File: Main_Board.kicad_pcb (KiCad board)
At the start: 2 copper layers, 95 x 95 mm, 61 parts, among them J1 DAC_12-bits, J2 Measurement_Header, Q1 Q_PNP_BCE, Q2 Q_NPN_BCE, U1 AD667, U2 LF356

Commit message: All traced
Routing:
- net /+15V: track 135.9 -> 210.0 mm, vias 1 -> 3
- net /-15V: track 118.5 -> 175.2 mm
- net GND: track 423.9 -> 480.5 mm
- net /Vout: track 13.5 -> 38.4 mm
- net /-5V: track 62.5 -> 69.4 mm, vias 0 -> 1
- net /-3V: track 77.0 -> 83.5 mm
- net Net-(RV1-Pad1): track 25.2 -> 29.2 mm
- net /Vin: track 199.4 -> 201.6 mm
- net Net-(RV1-Pad2): track 29.6 -> 31.2 mm
- net /MSP430_P1.6_Bit6: track 9.63 -> 9.00 mm

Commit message: Final
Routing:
- net GND: track 480.5 -> 492.6 mm
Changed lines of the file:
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@@
     (thickness 1.6)
     (drawings 17)
-    (tracks 481)
+    (tracks 482)
     (zones 0)
     (modules 61)
@@
   (segment (start 31.9 124.9) (end 37 130) (width 0.25) (layer F.Cu) (net 1))
   (segment (start 31.9 121.0375) (end 31.9 124.9) (width 0.25) (layer F.Cu) (net 1))
-  (segment (start 21.125 139.7) (end 18.7 142.125) (width 0.25) (layer F.Cu) (net 1))
   (segment (start 23.91 139.7) (end 21.125 139.7) (width 0.25) (layer F.Cu) (net 1))
   (segment (start 37 130.175997) (end 37 130) (width 0.25) (layer F.Cu) (net 1))
@@
   (segment (start 18.7 142.125) (end 22.5125 145.9375) (width 0.25) (layer F.Cu) (net 1))
   (segment (start 18.214473 142.610527) (end 18.7 142.125) (width 0.25) (layer F.Cu) (net 1))
-  (segment (start 17.67499 143.15001) (end 18.214473 142.610527) (width 0.25) (layer F.Cu) (net 1))
-  (segment (start 17.67499 144.47934) (end 17.67499 143.15001) (width 0.25) (layer F.Cu) (net 1))
-  (segment (start 21.09205 147.8964) (end 17.67499 144.47934) (width 0.25) (layer F.Cu) (net 1))
-  (segment (start 30.8508 147.8964) (end 21.09205 147.8964) (width 0.25) (layer F.Cu) (net 1))
   (segment (start 64.6826 117.5506) (end 64.7304 117.5028) (width 0.25) (layer F.Cu) (net 1))
   (segment (start 60.26 117.5506) (end 64.6826 117.5506) (width 0.25) (layer F.Cu) (net 1))
@@
   (segment (start 90.8658 112.1658) (end 80.5304 112.1658) (width 0.25) (layer F.Cu) (net 1))
   (segment (start 93.3 114.6) (end 90.8658 112.1658) (width 0.25) (layer F.Cu) (net 1))
-  (segment (start 34.894563 150.327637) (end 35.4508 149.7714) (width 0.25) (layer F.Cu) (net 2))
-  (segment (start 30.8508 149.7714) (end 31.407037 150.327637) (width 0.25) (layer F.Cu) (net 2))
+  (segment (start 17.2 139.7) (end 21.125 139.7) (width 0.25) (layer F.Cu) (net 1))
+  (segment (start 16.1 140.8) (end 17.2 139.7) (width 0.25) (layer F.Cu) (net 1))
+  (segment (start 16.1 145.5) (end 16.1 140.8) (width 0.25) (layer F.Cu) (net 1))
+  (segment (start 30.8508 147.8964) (end 18.4964 147.8964) (width 0.25) (layer F.Cu) (net 1))
+  (segment (start 18.4964 147.8964) (end 16.1 145.5) (width 0.25) (layer F.Cu) (net 1))
+  (segment (start 23.71 139.7) (end 23.91 139.7) (width 0.25) (layer F.Cu) (net 1))
+  (segment (start 21.285 142.125) (end 23.71 139.7) (width 0.25) (layer F.Cu) (net 1))
+  (segment (start 18.7 142.125) (end 21.285 142.125) (width 0.25) (layer F.Cu) (net 1))
   (via (at 43.0508 156.7714) (size 0.8) (drill 0.4) (layers F.Cu B.Cu) (net 2))
   (segment (start 45.5758 156.7714) (end 43.0508 156.7714) (width 0.25) (layer F.Cu) (net 2))
@@
   (segment (start 21.3336 146.6336) (end 32.1168 146.6336) (width 0.25) (layer F.Cu) (net 2))
   (segment (start 32.1168 146.6336) (end 32.5232 147.04) (width 0.25) (layer F.Cu) (net 2))
-  (segment (start 32.5232 147.04) (end 32.5232 150.3166) (width 0.25) (layer F.Cu) (net 2))
-  (segment (start 31.407037 150.327637) (end 32.5232 150.3166) (width 0.25) (layer F.Cu) (net 2))
-  (segment (start 32.5232 150.3166) (end 34.894563 150.327637) (width 0.25) (layer F.Cu) (net 2))
+  (segment (start 31.6508 149.7714) (end 35.4508 149.7714) (width 0.25) (layer F.Cu) (net 2))
+  (segment (start 30.8508 149.7714) (end 31.6508 149.7714) (width 0.25) (layer F.Cu) (net 2))
+  (segment (start 32.5232 148.099) (end 30.8508 149.7714) (width 0.25) (layer F.Cu) (net 2))
+  (segment (start 32.5232 147.04) (end 32.5232 148.099) (width 0.25) (layer F.Cu) (net 2))
   (segment (start 29.241333 141.416333) (end 29.19233 141.416333) (width 0.25) (layer F.Cu) (net 3))
   (segment (start 47.4508 150.9014) (end 47.4508 156.7714) (width 0.25) (layer F.Cu) (net 3))
@@
   (segment (start 54.2133 168.8714) (end 54.1508 168.8089) (width 0.25) (layer F.Cu) (net 3))
   (segment (start 61.2408 168.8714) (end 54.2133 168.8714) (width 0.25) (layer F.Cu) (net 3))
-  (segment (start 54.1508 169.6714) (end 54.1508 168.8089) (width 0.25) (layer F.Cu) (net 3))
-  (segment (start 58.7508 174.2714) (end 54.1508 169.6714) (width 0.25) (layer F.Cu) (net 3))
   (segment (start 78.2708 168.9714) (end 78.3708 168.8714) (width 0.25) (layer F.Cu) (net 3))
   (segment (start 73.6508 168.9714) (end 78.2708 168.9714) (width 0.25) (layer F.Cu) (net 3))
-  (segment (start 73.6508 168.9714) (end 73.6508 170.7714) (width 0.25) (layer F.Cu) (net 3))
-  (segment (start 73.6508 170.7714) (end 69.2508 175.1714) (width 0.25) (layer F.Cu) (net 3))
-  (segment (start 59.6508 175.1714) (end 58.7508 174.2714) (width 0.25) (layer F.Cu) (net 3))
-  (segment (start 69.2508 175.1714) (end 59.6508 175.1714) (width 0.25) (layer F.Cu) (net 3))
   (segment (start 50.58395 168.8089) (end 49.0508 167.27575) (width 0.25) (layer F.Cu) (net 3))
   (segment (start 54.1508 168.8089) (end 50.58395 168.8089) (width 0.25) (layer F.Cu) (net 3))
@@
   (segment (start 51.5478 141.8076) (end 52.113485 141.8076) (width 0.25) (layer B.Cu) (net 3))
   (segment (start 52.113485 141.8076) (end 57.105885 146.8) (width 0.25) (layer B.Cu) (net 3))
+  (segment (start 73.6508 170.7714) (end 73.6508 168.9714) (width 0.25) (layer F.Cu) (net 3))
+  (segment (start 68.8222 175.6) (end 73.6508 170.7714) (width 0.25) (layer F.Cu) (net 3))
+  (segment (start 60.0794 175.6) (end 68.8222 175.6) (width 0.25) (layer F.Cu) (net 3))
+  (segment (start 54.1508 168.8089) (end 54.1508 169.6714) (width 0.25) (layer F.Cu) (net 3))
+  (segment (start 54.1508 169.6714) (end 60.0794 175.6) (width 0.25) (layer F.Cu) (net 3))
   (segment (start 78.4508 163.8714) (end 80.9108 166.3314) (width 0.25) (layer F.Cu) (net 4))
   (segment (start 78.4508 158.8714) (end 78.4508 163.8714) (width 0.25) (layer F.Cu) (net 4))

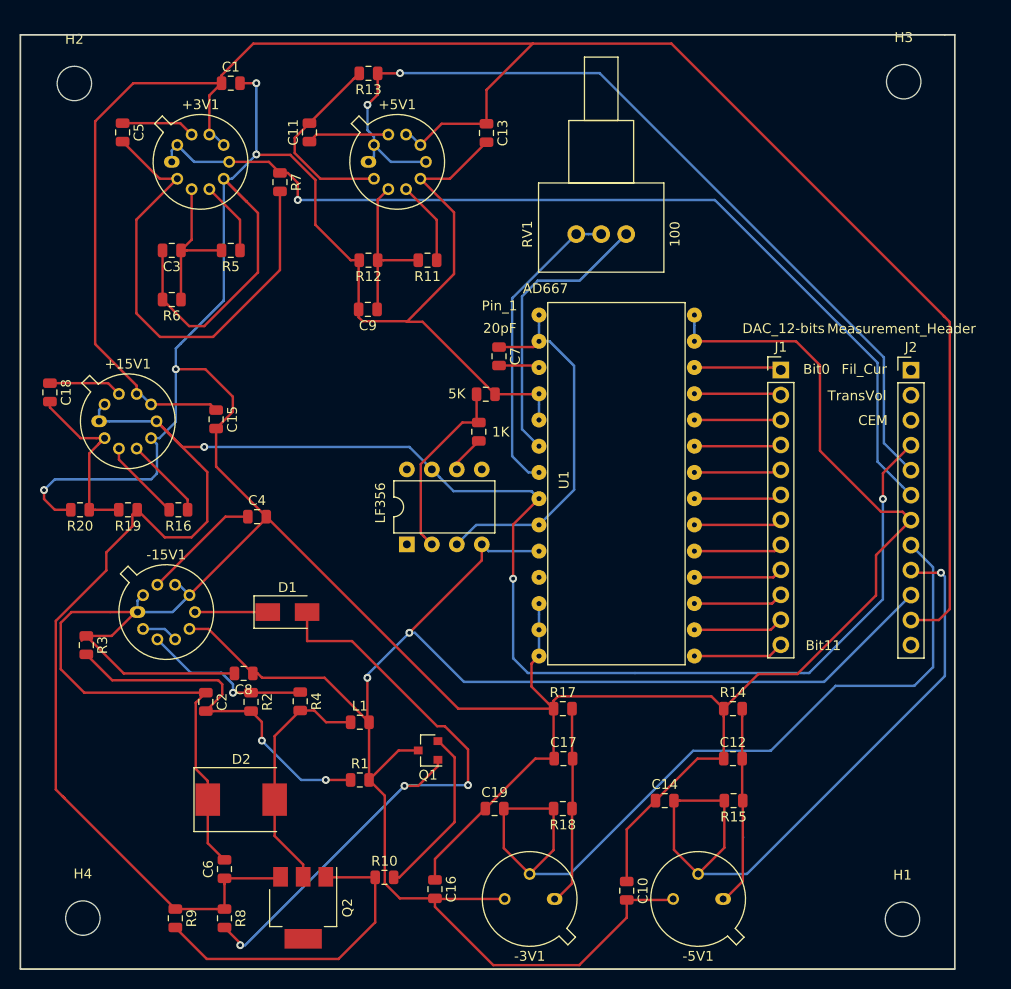
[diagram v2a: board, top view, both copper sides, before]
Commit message: Moved holes
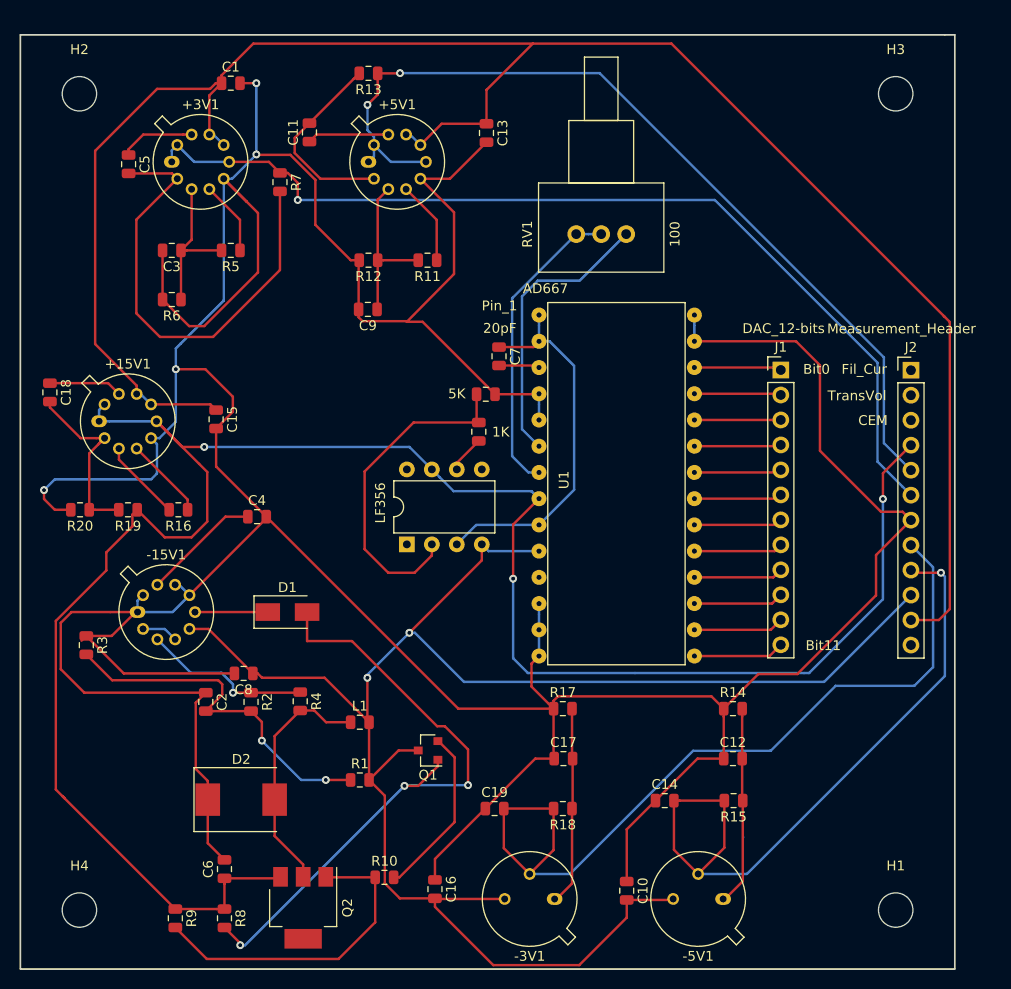
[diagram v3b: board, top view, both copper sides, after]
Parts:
- moved C5 3.30 mm to (23.0, 94.2)
- moved H3 1.47 mm to (101.0, 87.0)
- moved H2 1.17 mm to (18.0, 87.0)
- moved H1 1.17 mm to (101.0, 170.0)
- moved H4 0.89 mm to (18.0, 170.0)
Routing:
- net Net-(R21-Pad2): track 19.2 -> 34.2 mm
- net Net-(+3V1-Pad2): track 48.9 -> 47.0 mm
- net /Vin: track 201.6 -> 199.8 mm
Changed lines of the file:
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@@
     (thickness 1.6)
     (drawings 17)
-    (tracks 482)
+    (tracks 488)
     (zones 0)
     (modules 61)
@@
   )
   (module MountingHole:MountingHole_3.5mm (layer F.Cu)
-    (at 18.35 170.8144)
+    (at 18 170)
     (descr "Mounting Hole 3.5mm, no annular")
     (tags "mounting hole 3.5mm no annular")
@@
   )
   (module MountingHole:MountingHole_3.5mm (layer F.Cu)
-    (at 101.8144 85.7752)
+    (at 101 87)
     (descr "Mounting Hole 3.5mm, no annular")
     (tags "mounting hole 3.5mm no annular")
@@
   )
   (module MountingHole:MountingHole_3.5mm (layer F.Cu)
-    (at 17.4864 85.953)
+    (at 18 87)
     (descr "Mounting Hole 3.5mm, no annular")
     (tags "mounting hole 3.5mm no annular")
@@
   )
   (module MountingHole:MountingHole_3.5mm (layer F.Cu)
-    (at 101.6874 170.9414)
+    (at 101 170)
     (descr "Mounting Hole 3.5mm, no annular")
     (tags "mounting hole 3.5mm no annular")
@@
   )
   (module Capacitor_SMD:C_0805_2012Metric (layer F.Cu)
-    (at 22.3914 90.9238 270)
+    (at 23 94.1625 270)
     (descr "Capacitor SMD 0805 (2012 Metric), square (rectangular) end terminal, IPC_7351 nominal, (Body size source: https://docs.google.com/spreadsheets/d/1BsfQQcO9C6DZCsRaXUlFlo91Tg2WpOkGARC1WS5S8t0/edit?usp=sharing), generated with kicad-footprint-generator")
     (tags capacitor)
@@
   (segment (start 32.4539 85.1238) (end 35.6777 81.9) (width 0.25) (layer F.Cu) (net 6))
   (segment (start 32.4539 85.9238) (end 32.4539 85.1238) (width 0.25) (layer F.Cu) (net 6))
-  (segment (start 23.82233 116.674387) (end 19.6 112.452057) (width 0.25) (layer F.Cu) (net 6))
-  (segment (start 23.82233 117.522915) (end 23.82233 116.674387) (width 0.25) (layer F.Cu) (net 6))
-  (segment (start 19.6 112.452057) (end 19.6 89.8) (width 0.25) (layer F.Cu) (net 6))
-  (segment (start 23.4762 85.9238) (end 32.4539 85.9238) (width 0.25) (layer F.Cu) (net 6))
-  (segment (start 19.6 89.8) (end 23.4762 85.9238) (width 0.25) (layer F.Cu) (net 6))
   (segment (start 102.551 140.5122) (end 105.3878 140.5122) (width 0.25) (layer F.Cu) (net 6))
   (segment (start 105.3878 140.5122) (end 106.5 139.4) (width 0.25) (layer F.Cu) (net 6))
@@
   (segment (start 78.2 81.9) (end 105.9 109.6) (width 0.25) (layer F.Cu) (net 6))
   (segment (start 105.9 109.6) (end 106 109.7) (width 0.25) (layer F.Cu) (net 6))
+  (segment (start 23.82233 116.674387) (end 23.82233 117.522915) (width 0.25) (layer F.Cu) (net 6))
+  (segment (start 31.8664 85.9238) (end 31.2902 86.5) (width 0.25) (layer F.Cu) (net 6))
+  (segment (start 32.4539 85.9238) (end 31.8664 85.9238) (width 0.25) (layer F.Cu) (net 6))
+  (segment (start 31.2902 86.5) (end 25.9 86.5) (width 0.25) (layer F.Cu) (net 6))
+  (segment (start 25.9 86.5) (end 19.6 92.8) (width 0.25) (layer F.Cu) (net 6))
+  (segment (start 19.6 92.8) (end 19.6 112.452057) (width 0.25) (layer F.Cu) (net 6))
+  (segment (start 19.6 112.452057) (end 23.82233 116.674387) (width 0.25) (layer F.Cu) (net 6))
   (via (at 51.0508 157.3714) (size 0.8) (drill 0.4) (layers F.Cu B.Cu) (net 7))
   (segment (start 41.15 142.65) (end 41.15 139.7) (width 0.25) (layer F.Cu) (net 7))
@@
   (segment (start 29 128.254755) (end 23.82233 123.077085) (width 0.25) (layer F.Cu) (net 15))
   (segment (start 29 129.3) (end 29 128.254755) (width 0.25) (layer F.Cu) (net 15))
-  (segment (start 28.248655 89.9863) (end 29.40907 91.146715) (width 0.25) (layer F.Cu) (net 16))
-  (segment (start 22.3914 89.9863) (end 28.248655 89.9863) (width 0.25) (layer F.Cu) (net 16))
+  (segment (start 28.560542 91.146715) (end 29.40907 91.146715) (width 0.25) (layer F.Cu) (net 16))
+  (segment (start 24.490785 91.146715) (end 28.560542 91.146715) (width 0.25) (layer F.Cu) (net 16))
+  (segment (start 23 92.6375) (end 24.490785 91.146715) (width 0.25) (layer F.Cu) (net 16))
+  (segment (start 23 93.225) (end 23 92.6375) (width 0.25) (layer F.Cu) (net 16))
   (segment (start 34.3289 99.816055) (end 34.3289 102.9238) (width 0.25) (layer F.Cu) (net 17))
   (segment (start 31.21373 96.700885) (end 34.3289 99.816055) (width 0.25) (layer F.Cu) (net 17))
@@
   (segment (start 28.9164 102.9238) (end 32.4539 102.9238) (width 0.25) (layer F.Cu) (net 18))
   (segment (start 28.3289 102.9238) (end 28.9164 102.9238) (width 0.25) (layer F.Cu) (net 18))
-  (segment (start 26.170233 95.640133) (end 22.3914 91.8613) (width 0.25) (layer F.Cu) (net 19))
-  (segment (start 27.94907 95.640133) (end 26.170233 95.640133) (width 0.25) (layer F.Cu) (net 19))
   (segment (start 38.3914 96.9238) (end 38.3914 104.9238) (width 0.25) (layer F.Cu) (net 19))
   (segment (start 38.3914 104.9238) (end 31.5914 111.7238) (width 0.25) (layer F.Cu) (net 19))
@@
   (segment (start 23.7914 99.797803) (end 27.94907 95.640133) (width 0.25) (layer F.Cu) (net 19))
   (segment (start 23.7914 109.3238) (end 23.7914 99.797803) (width 0.25) (layer F.Cu) (net 19))
+  (segment (start 27.408937 95.1) (end 27.94907 95.640133) (width 0.25) (layer F.Cu) (net 19))
+  (segment (start 23 95.1) (end 27.408937 95.1) (width 0.25) (layer F.Cu) (net 19))
   (segment (start 42.105985 91.146715) (end 49.40907 91.146715) (width 0.25) (layer F.Cu) (net 20))
   (segment (start 41.3914 91.8613) (end 42.105985 91.146715) (width 0.25) (layer F.Cu) (net 20))
@@
   (segment (start 58.385 120.2014) (end 58.609 120.4254) (width 0.25) (layer F.Cu) (net 50))
   (segment (start 58.385 117.5506) (end 58.385 120.2014) (width 0.25) (layer F.Cu) (net 50))
-  (segment (start 52.708799 131.690999) (end 53.033801 132.016001) (width 0.25) (layer F.Cu) (net 50))
-  (segment (start 52.708799 124.655999) (end 52.708799 131.690999) (width 0.25) (layer F.Cu) (net 50))
-  (segment (start 56.939398 120.4254) (end 52.708799 124.655999) (width 0.25) (layer F.Cu) (net 50))
-  (segment (start 53.033801 132.016001) (end 53.8338 132.816) (width 0.25) (layer F.Cu) (net 50))
-  (segment (start 58.609 120.4254) (end 56.939398 120.4254) (width 0.25) (layer F.Cu) (net 50))
+  (segment (start 53.8338 133.94737) (end 52.08117 135.7) (width 0.25) (layer F.Cu) (net 50))
+  (segment (start 53.8338 132.816) (end 53.8338 133.94737) (width 0.25) (layer F.Cu) (net 50))
+  (segment (start 52.08117 135.7) (end 49.4 135.7) (width 0.25) (layer F.Cu) (net 50))
+  (segment (start 49.4 135.7) (end 47 133.3) (width 0.25) (layer F.Cu) (net 50))
+  (segment (start 47 133.3) (end 47 125.4) (width 0.25) (layer F.Cu) (net 50))
+  (segment (start 51.9746 120.4254) (end 58.609 120.4254) (width 0.25) (layer F.Cu) (net 50))
+  (segment (start 47 125.4) (end 51.9746 120.4254) (width 0.25) (layer F.Cu) (net 50))
   (segment (start 56.3738 124.5356) (end 56.3738 125.196) (width 0.25) (layer F.Cu) (net 51))
   (segment (start 58.609 122.3004) (end 56.3738 124.5356) (width 0.25) (layer F.Cu) (net 51))

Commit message: Layout
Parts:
- moved J1 0.69 mm to (90.0, 115.0)
- moved J2 0.56 mm to (102.0, 115.0)
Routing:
- net /MSP430_P2.3_Bit11: track 9.26 -> 9.98 mm
- net /MSP430_P2.0_Bit8: track 9.10 -> 9.82 mm
- net /MSP430_P1.7_Bit7: track 9.05 -> 9.77 mm
- net /MSP430_P1.5_Bit5: track 8.95 -> 9.66 mm
- net /MSP430_P1.4_Bit4: track 8.89 -> 9.61 mm
- net /MSP430_P1.2_Bit2: track 8.79 -> 9.51 mm
- net /MSP430_P1.3_Bit3: track 8.84 -> 9.56 mm
- net /MSP430_P2.2_Bit10: track 9.21 -> 9.93 mm
- net /MSP430_P2.1_Bit9: track 9.16 -> 9.87 mm
- net /MSP430_P1.6_Bit6: track 9.00 -> 9.72 mm
- net GND: track 492.6 -> 491.9 mm
- net /MSP430_P1.0_Bit0: track 8.89 -> 9.54 mm
- net /MSP430_P1.1_Bit1: track 8.84 -> 9.49 mm
- net /-5V: track 69.4 -> 70.0 mm
- net /Vin: track 199.8 -> 200.3 mm
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
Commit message: Final Changes
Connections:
- J2 pad 12: Net-(J2-Pad12) -> /GridStack
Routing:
- net /GridStack: track 3.82 -> 77.9 mm, vias 0 -> 1

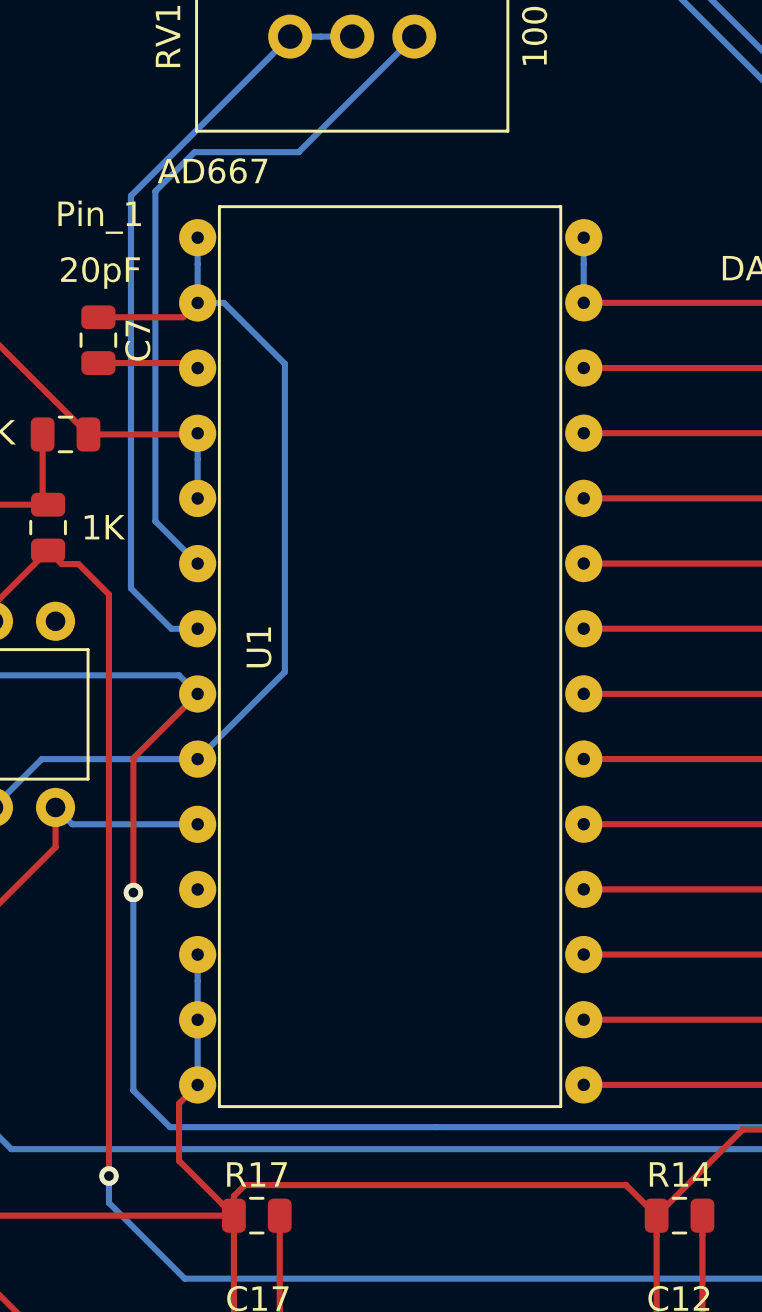
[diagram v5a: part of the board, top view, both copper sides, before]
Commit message: Needed to update sizing of DAC pin holes to 1.02mm, caught my initial error.
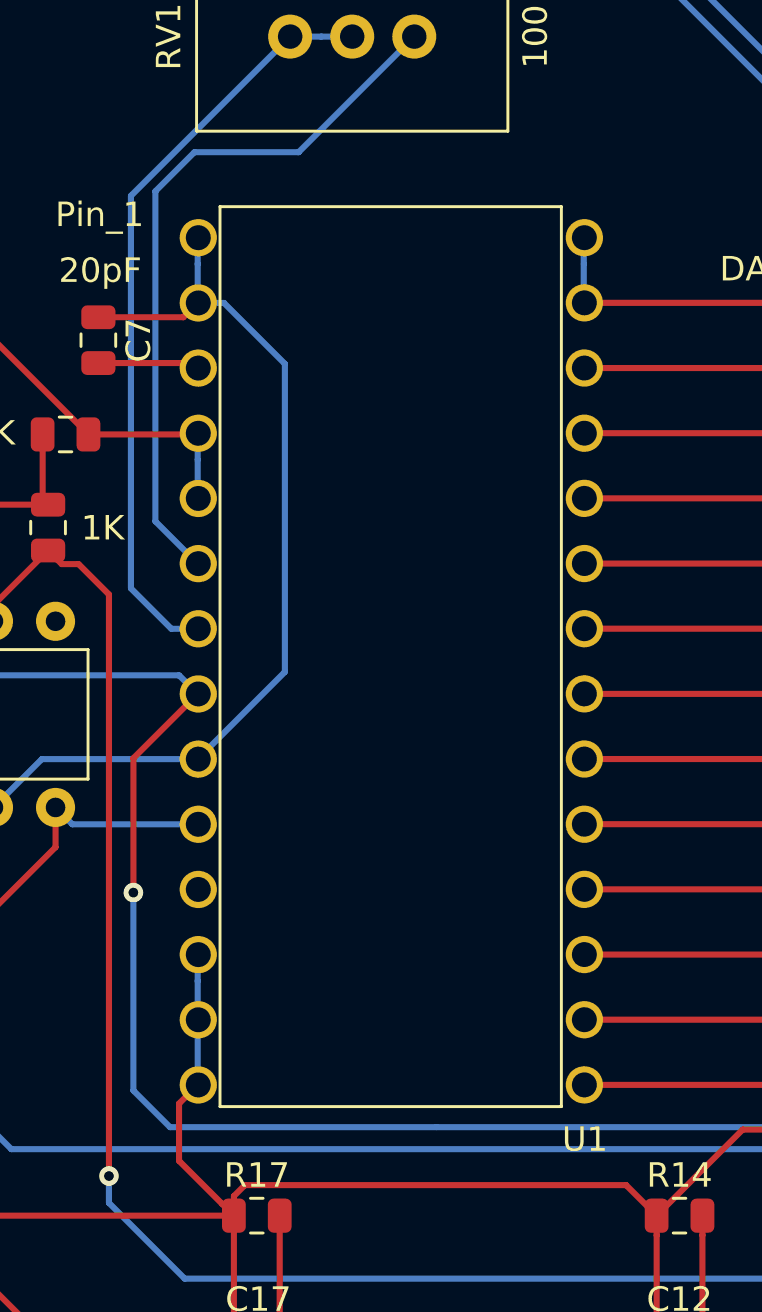
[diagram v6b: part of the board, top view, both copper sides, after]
